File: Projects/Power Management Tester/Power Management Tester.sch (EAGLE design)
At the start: 13 parts

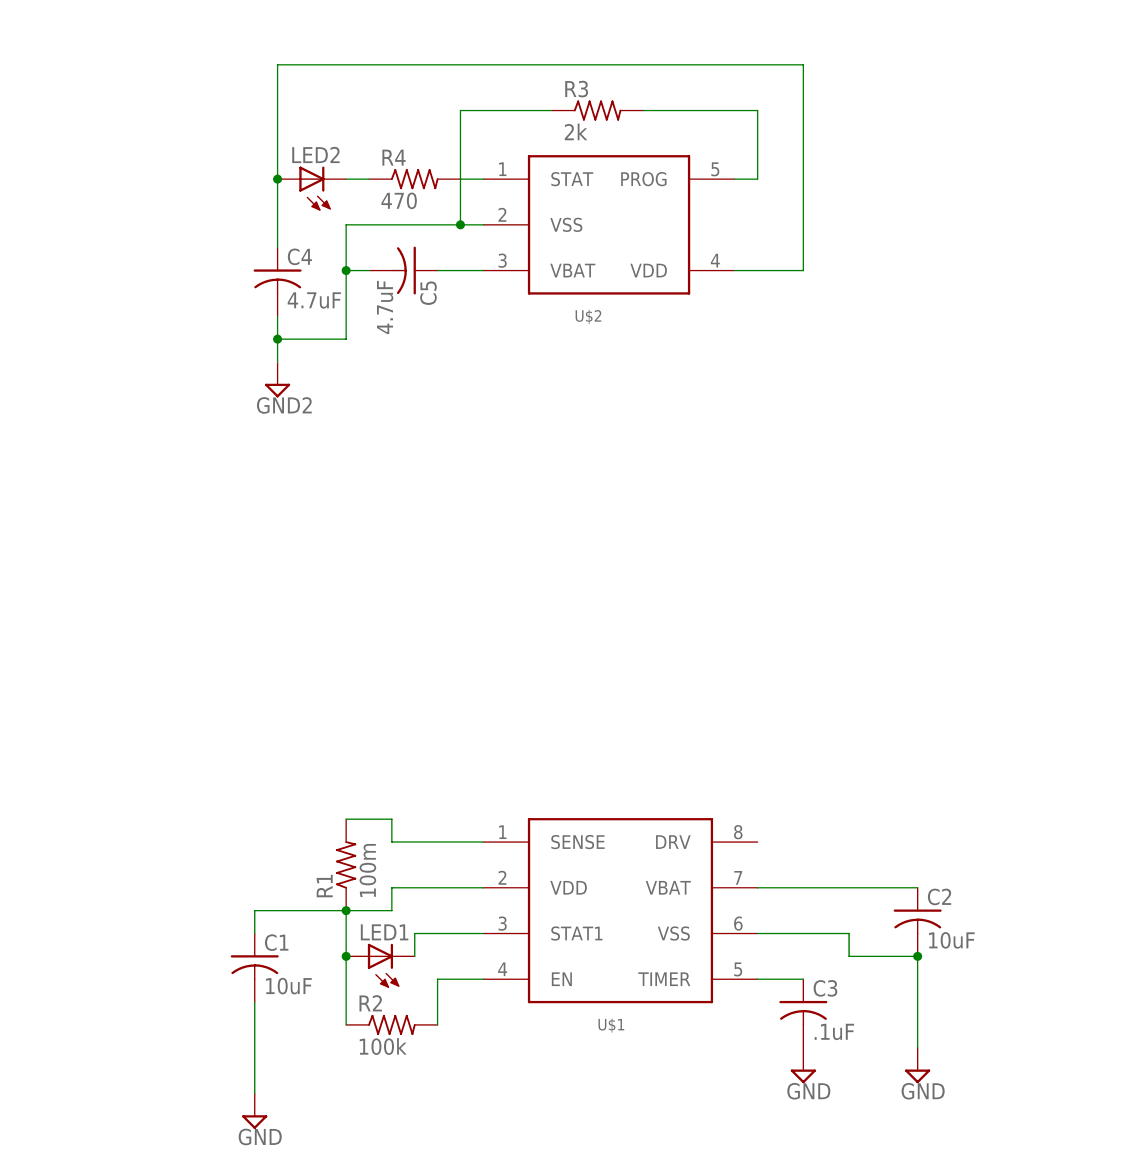
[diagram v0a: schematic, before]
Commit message: added battery management parts
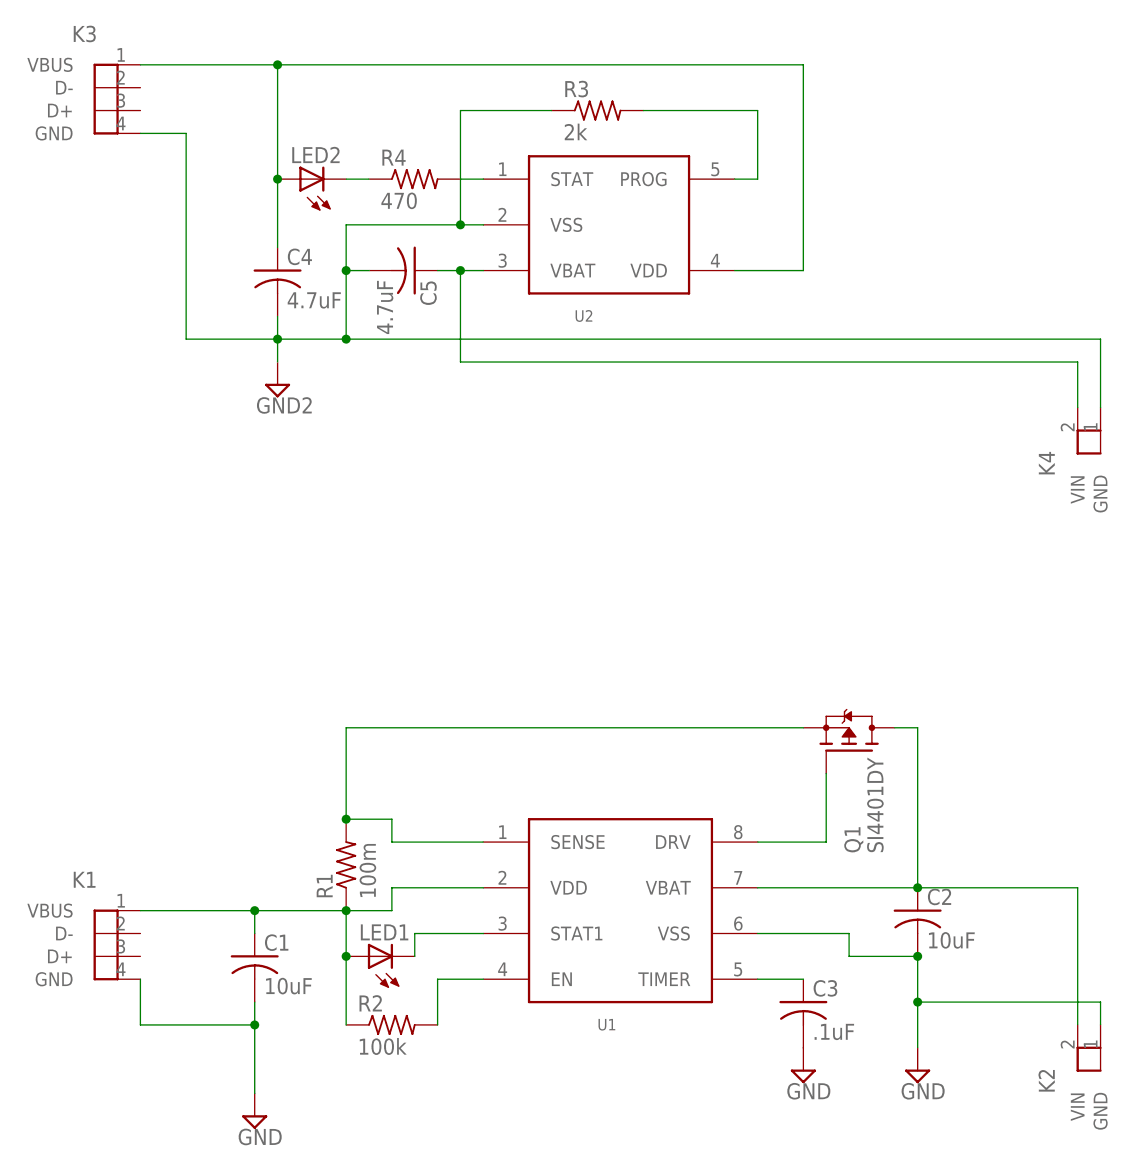
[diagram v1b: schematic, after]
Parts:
- added K1, K3: USBCONN, lightsuits:USBCONN
- added K2, K4: PWRCONN, lightsuits:PWRCONN
- added Q1: SI4401DY, lightsuits:SI4401DY
- renumbered U$1 to U1, U$2 to U2
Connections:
- removed net C1: C1.1, LED1.POS, R1.1, R2.1, U1.VDD
- removed net C2: C2.1, U1.VBAT
- removed net GND: C1.2, C2.2, C3.2, U1.VSS
- removed net N$2: C4.1, LED2.POS, U2.VDD
- new net 5V_1: C1.1, K1.VBUS, LED1.POS, R1.1, R2.1, U1.VDD
- new net 5V_2: C4.1, K3.VBUS, LED2.POS, U2.VDD
- new net D: C2.1, K2.VIN, Q1.D, U1.VBAT
- new net GND1: C1.2, C2.2, C3.2, K1.GND, K2.GND, U1.VSS
- new net N$9: Q1.G, U1.DRV
- net GND2: now also K3.GND, K4.GND
- net N$5: now also Q1.S
- net N$8: now also K4.VIN
